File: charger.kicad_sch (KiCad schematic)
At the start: 37 parts, among them Q1 NMOS, Q2 NMOS, U2 BQ25798RQMR

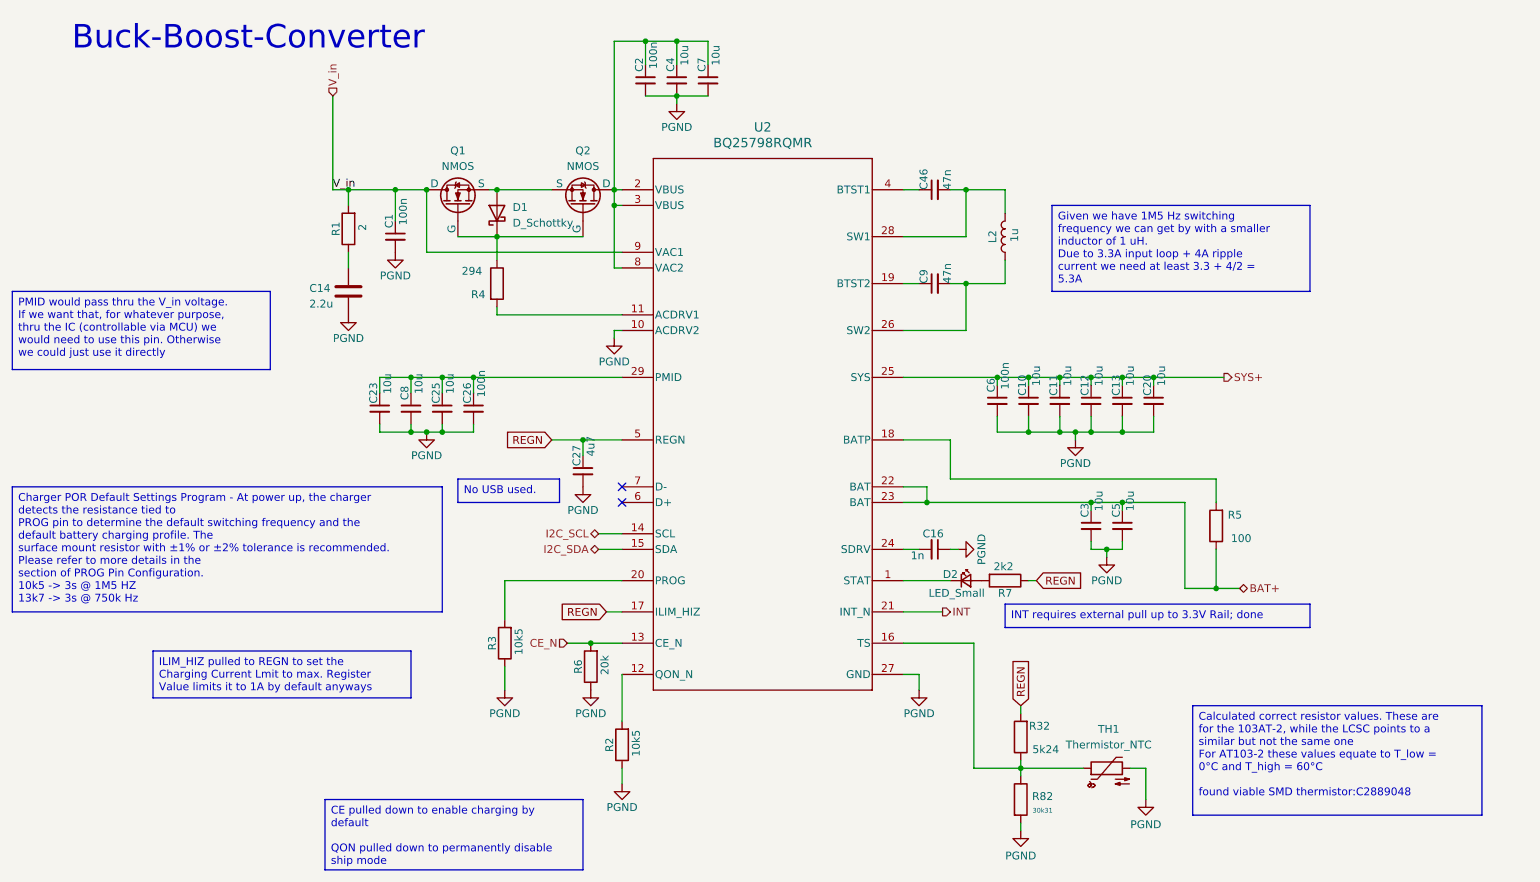
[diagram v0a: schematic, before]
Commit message: added missing footprints and validated all lcsc numbers; started pcb-layouting
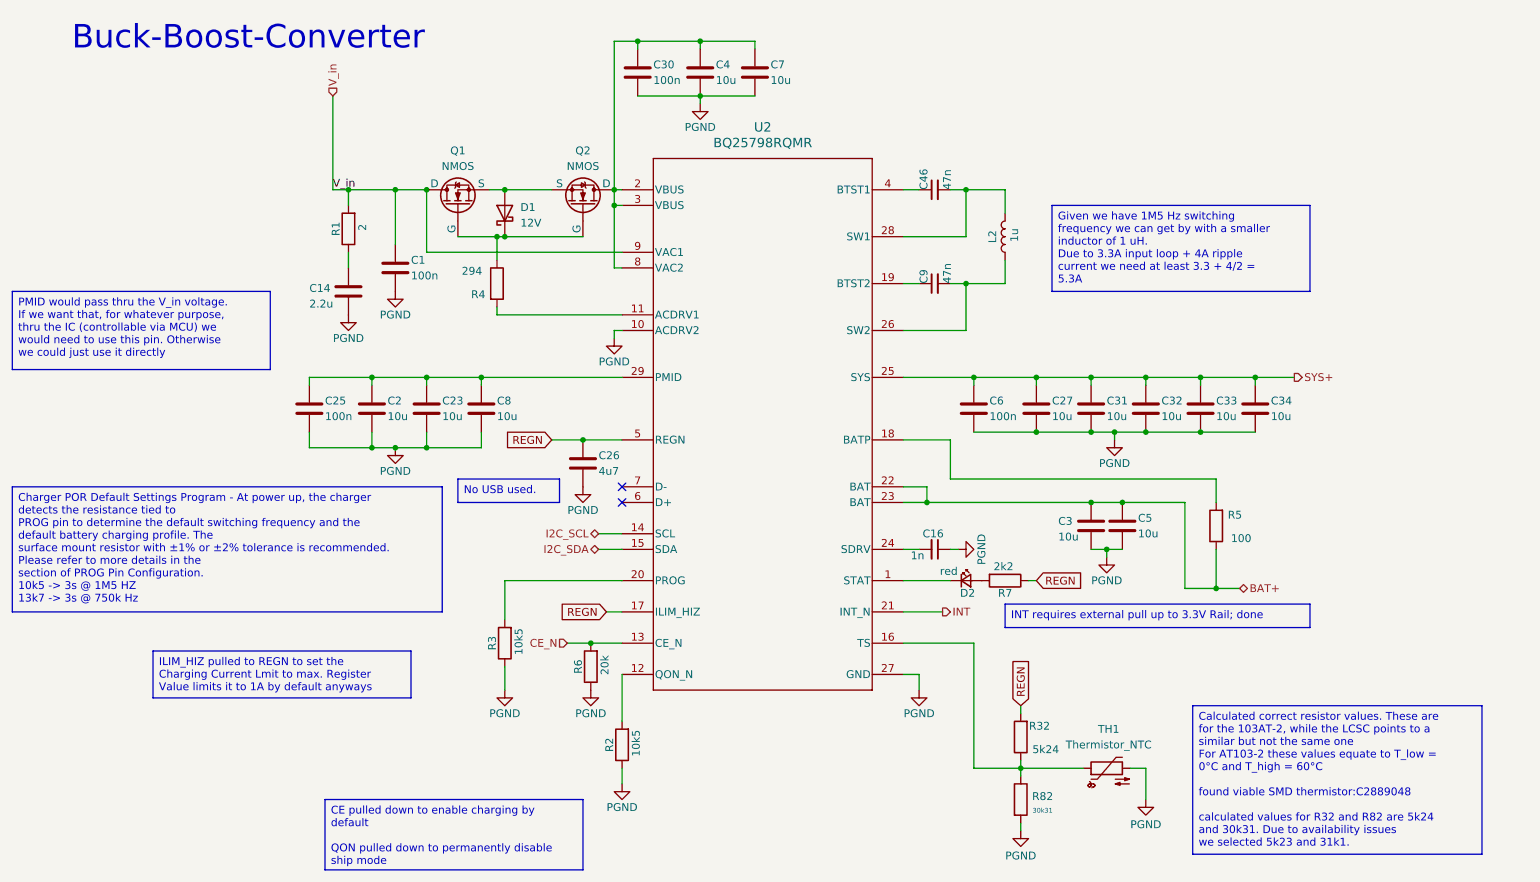
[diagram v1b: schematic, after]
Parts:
- removed C1, C2, C26, C6: 100n, Capacitor_SMD:C_0402_1005Metric, symbol Device:C_Small
- removed C10, C11, C12, C13, C20, C23, C25, C3, C4, C5, C7, C8: 10u, Capacitor_SMD:C_0402_1005Metric, symbol Device:C_Small
- removed C27: 4u7, Capacitor_SMD:C_0402_1005Metric, symbol Device:C_Small
- added C1, C25, C30, C6: 100n, Capacitor_SMD:C_0402_1005Metric, symbol Device:C
- added C2, C23, C27, C3, C31, C32, C33, C34, C4, C5, C7, C8: 10u, Capacitor_SMD:C_0603_1608Metric, symbol Device:C
- added C26: 4u7, Capacitor_SMD:C_0402_1005Metric, symbol Device:C
- C14: footprint (none) -> Capacitor_SMD:C_0805_2012Metric; LCSC (none) -> C377773
- D1: value D_Schottky -> 12V; footprint (none) -> Diode_SMD:D_SOD-523; LCSC (none) -> C507911
- D2: value LED_Small -> red; footprint (none) -> LED_SMD:LED_0603_1608Metric; LCSC (none) -> C2286
- Q1, Q2: footprint (none) -> Package_TO_SOT_THT:TO-220-3_Horizontal_TabDown; LCSC (none) -> C5297496
- R1: footprint Resistor_SMD:R_0402_1005Metric -> Resistor_SMD:R_0603_1608Metric; LCSC (none) -> C22977
- R2, R3: footprint Resistor_SMD:R_0402_1005Metric -> Resistor_SMD:R_0603_1608Metric; LCSC (none) -> C22855
- R32: LCSC C25900 -> C23068
- R4: LCSC C25900 -> C22990
- R5: LCSC C25900 -> C22775
- R6: footprint Resistor_SMD:R_0402_1005Metric -> Resistor_SMD:R_0603_1608Metric; LCSC (none) -> C4184
- R7: footprint Resistor_SMD:R_0402_1005Metric -> Resistor_SMD:R_0603_1608Metric; LCSC (none) -> C4190
- R82: footprint Resistor_SMD:R_0603_1608Metric -> Resistor_SMD:R_0805_2012Metric; LCSC C25768 -> C21841
- TH1: footprint Capacitor_SMD:C_0201_0603Metric -> Resistor_SMD:R_0603_1608Metric
- U2: footprint RQM0029A-MFG -> BQ25798:IC_BQ25798RQMR; LCSC (none) -> C2876593
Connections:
- net BAT+: now also C3.1, C5.1
- net PGND: now also C1.2, C2.2, C23.2, C25.2, C26.2, C27.2, C3.2, C30.2, C31.2, C32.2, C33.2, C34.2, C4.2, C5.2, C6.2, C7.2, C8.2
- net REGN: now also C26.1
- net SYS+: now also C27.1, C31.1, C32.1, C33.1, C34.1, C6.1
- net V_in: now also C1.1
- net at Q2.1 (D), U2.2 (VBUS), U2.3 (VBUS)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: now also C30.1, C4.1, C7.1
- net at U2.29 (PMID): now also C2.1, C23.1, C25.1, C8.1
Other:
- moved on the sheet: D1

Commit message: started routing Please enter the commit message for your changes. Lines starting
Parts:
- removed D1: 12V, Diode_SMD:D_SOD-523, symbol Device:D_Schottky
- removed Q1, Q2: NMOS, Package_TO_SOT_THT:TO-220-3_Horizontal_TabDown, symbol Simulation_SPICE:NMOS
- removed R4: 294, Resistor_SMD:R_0603_1608Metric, symbol Device:R
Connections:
- net PGND: now also U2.11 (ACDRV1)
- net V_in: now also C30.1, C4.1, C7.1, U2.2 (VBUS), U2.3 (VBUS), U2.8 (VAC2)
